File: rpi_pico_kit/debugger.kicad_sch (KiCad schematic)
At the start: 39 parts, among them J3 USB_B, U2 RP2040, U3 NCP1117-3.3_SOT223, U4 W25Q128JVS, Y1 12MHz

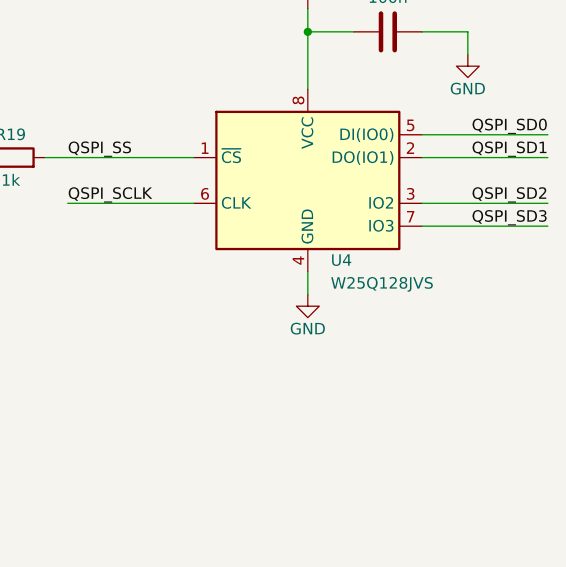
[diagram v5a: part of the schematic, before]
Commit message: added MPNs for capacitors
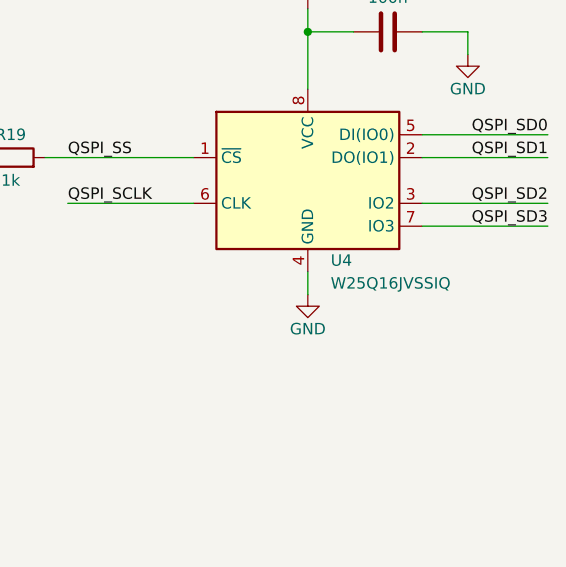
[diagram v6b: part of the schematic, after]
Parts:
- C10, C11, C12, C18, C3, C4, C6, C7, C8, C9: Manufacturer Part Number (none) -> C0805C104M3RAC7800; Supplier (none) -> Digikey; Supplier Part URL (none) -> https://www.digikey.cz/en/products/detail/kemet/C0805C104M3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
- C13, C5: Manufacturer Part Number (none) -> C0805C105Z4VAC7800; Supplier (none) -> Digikey; Supplier Part URL (none) -> https://www.digikey.cz/en/products/detail/kemet/C0805C105Z4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
- C14, C15: Manufacturer Part Number (none) -> C0805C120J1HAC7800; Supplier (none) -> Digikey; Supplier Part URL (none) -> https://www.digikey.cz/en/products/detail/kemet/C0805C120J1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
- C16, C17: Manufacturer Part Number (none) -> CL21A106KOQNNNG; Supplier (none) -> Digikey; Supplier Part URL (none) -> https://www.digikey.cz/en/products/detail/samsung-electro-m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
- U4: value W25Q128JVS -> W25Q16JVSSIQ; Manufacturer Part Number (none) -> W25Q16JVSSIQ; Supplier (none) -> Digikey; Supplier Part URL (none) -> https://www.digikey.cz/cs/products/detail/winbond-electroni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
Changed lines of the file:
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@@
+      (effects (font (size 1.27 1.27)) hide)
+    )
+    (property "Manufacturer Part Number" "C0805C104M3RAC7800" (id 4) (at 170.18 34.29 0)
+      (effects (font (size 1.27 1.27)) hide)
+    )
+    (property "Supplier" "Digikey" (id 5) (at 170.18 34.29 0)
+      (effects (font (size 1.27 1.27)) hide)
+    )
+    (property "Supplier Part URL" "https://www.digikey.cz/en/products/detail/kemet/C0805C104M3RAC7800/2211748" (id 6) (at 170.18 34.29 0)
       (effects (font (size 1.27 1.27)) hide)
     )
@@
       (effects (font (size 1.27 1.27)) hide)
     )
+    (property "Manufacturer Part Number" "C0805C104M3RAC7800" (id 4) (at 135.89 34.29 0)
+      (effects (font (size 1.27 1.27)) hide)
+    )
+    (property "Supplier" "Digikey" (id 5) (at 135.89 34.29 0)
+      (effects (font (size 1.27 1.27)) hide)
+    )
+    (property "Supplier Part URL" "https://www.digikey.cz/en/products/detail/kemet/C0805C104M3RAC7800/2211748" (id 6) (at 135.89 34.29 0)
+      (effects (font (size 1.27 1.27)) hide)
+    )
     (pin "1")
     (pin "2")
@@
       (effects (font (size 1.27 1.27)) hide)
     )
+    (property "Manufacturer Part Number" "C0805C104M3RAC7800" (id 4) (at 124.46 34.29 0)
+      (effects (font (size 1.27 1.27)) hide)
+    )
+    (property "Supplier" "Digikey" (id 5) (at 124.46 34.29 0)
+      (effects (font (size 1.27 1.27)) hide)
+    )
+    (property "Supplier Part URL" "https://www.digikey.cz/en/products/detail/kemet/C0805C104M3RAC7800/2211748" (id 6) (at 124.46 34.29 0)
+      (effects (font (size 1.27 1.27)) hide)
+    )
     (pin "1")
     (pin "2")
@@
       (effects (font (size 1.27 1.27)) hide)
     )
+    (property "Manufacturer Part Number" "C0805C104M3RAC7800" (id 4) (at 113.03 34.29 0)
+      (effects (font (size 1.27 1.27)) hide)
+    )
+    (property "Supplier" "Digikey" (id 5) (at 113.03 34.29 0)
+      (effects (font (size 1.27 1.27)) hide)
+    )
+    (property "Supplier Part URL" "https://www.digikey.cz/en/products/detail/kemet/C0805C104M3RAC7800/2211748" (id 6) (at 113.03 34.29 0)
+      (effects (font (size 1.27 1.27)) hide)
+    )
     (pin "1")
     (pin "2")
@@
     )
     (property "Datasheet" "~" (id 3) (at 44.45 48.26 0)
+      (effects (font (size 1.27 1.27)) hide)
+    )
+    (property "Manufacturer Part Number" "C0805C105Z4VAC7800" (id 4) (at 44.45 48.26 0)
+      (effects (font (size 1.27 1.27)) hide)
+    )
+    (property "Supplier" "Digikey" (id 5) (at 44.45 48.26 0)
+      (effects (font (size 1.27 1.27)) hide)
+    )
+    (property "Supplier Part URL" "https://www.digikey.cz/en/products/detail/kemet/C0805C105Z4VAC7800/2211782" (id 6) (at 44.45 48.26 0)
       (effects (font (size 1.27 1.27)) hide)
     )
@@
     )
     (property "Datasheet" "~" (id 3) (at 228.6 46.99 0)
+      (effects (font (size 1.27 1.27)) hide)
+    )
+    (property "Manufacturer Part Number" "CL21A106KOQNNNG" (id 4) (at 228.6 46.99 0)
+      (effects (font (size 1.27 1.27)) hide)
+    )
+    (property "Supplier" "Digikey" (id 5) (at 228.6 46.99 0)
+      (effects (font (size 1.27 1.27)) hide)
+    )
+    (property "Supplier Part URL" "https://www.digikey.cz/en/products/detail/samsung-electro-mechanics/CL21A106KOQNNNG/3894417" (id 6) (at 228.6 46.99 0)
       (effects (font (size 1.27 1.27)) hide)
     )
@@
       (effects (font (size 1.27 1.27)) hide)
     )
+    (property "Manufacturer Part Number" "C0805C104M3RAC7800" (id 4) (at 147.32 34.29 0)
+      (effects (font (size 1.27 1.27)) hide)
+    )
+    (property "Supplier" "Digikey" (id 5) (at 147.32 34.29 0)
+      (effects (font (size 1.27 1.27)) hide)
+    )
+    (property "Supplier Part URL" "https://www.digikey.cz/en/products/detail/kemet/C0805C104M3RAC7800/2211748" (id 6) (at 147.32 34.29 0)
+      (effects (font (size 1.27 1.27)) hide)
+    )
     (pin "1")
     (pin "2")
@@
       (effects (font (size 1.27 1.27)) hide)
     )
+    (property "Manufacturer Part Number" "C0805C104M3RAC7800" (id 4) (at 158.75 34.29 0)
+      (effects (font (size 1.27 1.27)) hide)
+    )
+    (property "Supplier" "Digikey" (id 5) (at 158.75 34.29 0)
+      (effects (font (size 1.27 1.27)) hide)
+    )
+    (property "Supplier Part URL" "https://www.digikey.cz/en/products/detail/kemet/C0805C104M3RAC7800/2211748" (id 6) (at 158.75 34.29 0)
+      (effects (font (size 1.27 1.27)) hide)
+    )
     (pin "1")
     (pin "2")
@@
       (effects (font (size 1.27 1.27)) hide)
     )
+    (property "Manufacturer Part Number" "C0805C120J1HAC7800" (id 4) (at 132.08 171.45 0)
+      (effects (font (size 1.27 1.27)) hide)
+    )
+    (property "Supplier" "Digikey" (id 5) (at 132.08 171.45 0)
+      (effects (font (size 1.27 1.27)) hide)
+    )
+    (property "Supplier Part URL" "https://www.digikey.cz/en/products/detail/kemet/C0805C120J1HAC7800/7948525" (id 6) (at 132.08 171.45 0)
+      (effects (font (size 1.27 1.27)) hide)
+    )
     (pin "1")
     (pin "2")
@@
     )
     (property "Datasheet" "~" (id 3) (at 101.6 34.29 0)
+      (effects (font (size 1.27 1.27)) hide)
+    )
+    (property "Manufacturer Part Number" "C0805C104M3RAC7800" (id 4) (at 101.6 34.29 0)
+      (effects (font (size 1.27 1.27)) hide)
+    )
+    (property "Supplier" "Digikey" (id 5) (at 101.6 34.29 0)
+      (effects (font (size 1.27 1.27)) hide)
+    )
+    (property "Supplier Part URL" "https://www.digikey.cz/en/products/detail/kemet/C0805C104M3RAC7800/2211748" (id 6) (at 101.6 34.29 0)
       (effects (font (size 1.27 1.27)) hide)
     )
@@
       (effects (font (size 1.27 1.27)) hide)
     )
+    (property "Manufacturer Part Number" "C0805C120J1HAC7800" (id 4) (at 132.08 184.15 0)
+      (effects (font (size 1.27 1.27)) hide)
+    )
+    (property "Supplier" "Digikey" (id 5) (at 132.08 184.15 0)
+      (effects (font (size 1.27 1.27)) hide)
+    )
+    (property "Supplier Part URL" "https://www.digikey.cz/en/products/detail/kemet/C0805C120J1HAC7800/7948525" (id 6) (at 132.08 184.15 0)
+      (effects (font (size 1.27 1.27)) hide)
+    )
     (pin "1")
     (pin "2")
@@
     )
     (property "Datasheet" "~" (id 3) (at 33.02 34.29 0)
+      (effects (font (size 1.27 1.27)) hide)
+    )
+    (property "Manufacturer Part Number" "C0805C104M3RAC7800" (id 4) (at 33.02 34.29 0)
+      (effects (font (size 1.27 1.27)) hide)
+    )
+    (property "Supplier" "Digikey" (id 5) (at 33.02 34.29 0)
+      (effects (font (size 1.27 1.27)) hide)
+    )
+    (property "Supplier Part URL" "https://www.digikey.cz/en/products/detail/kemet/C0805C104M3RAC7800/2211748" (id 6) (at 33.02 34.29 0)
       (effects (font (size 1.27 1.27)) hide)
     )
@@
       (effects (font (size 1.27 1.27)) hide)
     )
+    (property "Manufacturer Part Number" "C0805C104M3RAC7800" (id 4) (at 44.45 34.29 0)
+      (effects (font (size 1.27 1.27)) hide)
+    )
+    (property "Supplier" "Digikey" (id 5) (at 44.45 34.29 0)
+      (effects (font (size 1.27 1.27)) hide)
+    )
+    (property "Supplier Part URL" "https://www.digikey.cz/en/products/detail/kemet/C0805C104M3RAC7800/2211748" (id 6) (at 44.45 34.29 0)
+      (effects (font (size 1.27 1.27)) hide)
+    )
     (pin "1")
     (pin "2")
@@
       (effects (font (size 1.27 1.27)) hide)
     )
+    (property "Manufacturer Part Number" "CL21A106KOQNNNG" (id 4) (at 256.54 46.99 0)
+      (effects (font (size 1.27 1.27)) hide)
+    )
+    (property "Supplier" "Digikey" (id 5) (at 256.54 46.99 0)
+      (effects (font (size 1.27 1.27)) hide)
+    )
+    (property "Supplier Part URL" "https://www.digikey.cz/en/products/detail/samsung-electro-mechanics/CL21A106KOQNNNG/3894417" (id 6) (at 256.54 46.99 0)
+      (effects (font (size 1.27 1.27)) hide)
+    )
     (pin "1")
     (pin "2")
@@
       (effects (font (size 1.27 1.27)) hide)
     )
+    (property "Manufacturer Part Number" "C0805C104M3RAC7800" (id 4) (at 246.38 111.76 0)
+      (effects (font (size 1.27 1.27)) hide)
+    )
+    (property "Supplier" "Digikey" (id 5) (at 246.38 111.76 0)
+      (effects (font (size 1.27 1.27)) hide)
+    )
+    (property "Supplier Part URL" "https://www.digikey.cz/en/products/detail/kemet/C0805C104M3RAC7800/2211748" (id 6) (at 246.38 111.76 0)
+      (effects (font (size 1.27 1.27)) hide)
+    )
     (pin "1")
     (pin "2")
@@
     )
     (property "Datasheet" "~" (id 3) (at 101.6 48.26 0)
+      (effects (font (size 1.27 1.27)) hide)
+    )
+    (property "Manufacturer Part Number" "C0805C105Z4VAC7800" (id 4) (at 101.6 48.26 0)
+      (effects (font (size 1.27 1.27)) hide)
+    )
+    (property "Supplier" "Digikey" (id 5) (at 101.6 48.26 0)
+      (effects (font (size 1.27 1.27)) hide)
+    )
+    (property "Supplier Part URL" "https://www.digikey.cz/en/products/detail/kemet/C0805C105Z4VAC7800/2211782" (id 6) (at 101.6 48.26 0)
       (effects (font (size 1.27 1.27)) hide)
     )
@@
       (effects (font (size 1.27 1.27)) (justify left))
     )
-    (property "Value" "W25Q128JVS" (id 1) (at 240.03 139.7 0)
+    (property "Value" "W25Q16JVSSIQ" (id 1) (at 240.03 139.7 0)
       (effects (font (size 1.27 1.27)) (justify left))
     )
@@
       (effects (font (size 1.27 1.27)) hide)
     )
+    (property "Manufacturer Part Number" "W25Q16JVSSIQ" (id 4) (at 237.49 128.27 0)
+      (effects (font (size 1.27 1.27)) hide)
+    )
+    (property "Supplier" "Digikey" (id 5) (at 237.49 128.27 0)
+      (effects (font (size 1.27 1.27)) hide)
+    )
+    (property "Supplier Part URL" "https://www.digikey.cz/cs/products/detail/winbond-electronics/W25Q16JVSSIQ/6193769" (id 6) (at 237.49 128.27 0)
+      (effects (font (size 1.27 1.27)) hide)
+    )

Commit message: added MPNs for resistors
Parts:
- R10, R11: Manufacturer Part Number (none) -> RC0805FR-0727RL; Supplier (none) -> Digikey; Supplier Part URL (none) -> https://www.digikey.cz/en/products/detail/yageo/RC0805FR-07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
- R12, R13, R16, R17, R18, R19, R24, R27: Manufacturer Part Number (none) -> RC0805FR-071KL; Supplier (none) -> Digikey; Supplier Part URL (none) -> https://www.digikey.cz/en/products/detail/yageo/RC0805FR-07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
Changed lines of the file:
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@@
+      (effects (font (size 1.27 1.27)) hide)
+    )
+    (property "Manufacturer Part Number" "RC0805FR-071KL" (id 4) (at 154.94 184.15 0)
+      (effects (font (size 1.27 1.27)) hide)
+    )
+    (property "Supplier Part URL" "https://www.digikey.cz/en/products/detail/yageo/RC0805FR-071KL/727444" (id 5) (at 154.94 184.15 0)
+      (effects (font (size 1.27 1.27)) hide)
+    )
+    (property "Supplier" "Digikey" (id 6) (at 154.94 184.15 0)
       (effects (font (size 1.27 1.27)) hide)
     )
@@
     )
     (property "Datasheet" "~" (id 3) (at 120.65 67.31 0)
+      (effects (font (size 1.27 1.27)) hide)
+    )
+    (property "Manufacturer Part Number" "RC0805FR-0727RL" (id 4) (at 120.65 67.31 0)
+      (effects (font (size 1.27 1.27)) hide)
+    )
+    (property "Supplier Part URL" "https://www.digikey.cz/en/products/detail/yageo/RC0805FR-0727RL/727779" (id 5) (at 120.65 67.31 0)
+      (effects (font (size 1.27 1.27)) hide)
+    )
+    (property "Supplier" "Digikey" (id 6) (at 120.65 67.31 0)
       (effects (font (size 1.27 1.27)) hide)
     )
@@
       (effects (font (size 1.27 1.27)) hide)
     )
+    (property "Manufacturer Part Number" "RC0805FR-071KL" (id 4) (at 204.47 125.73 0)
+      (effects (font (size 1.27 1.27)) hide)
+    )
+    (property "Supplier Part URL" "https://www.digikey.cz/en/products/detail/yageo/RC0805FR-071KL/727444" (id 5) (at 204.47 125.73 0)
+      (effects (font (size 1.27 1.27)) hide)
+    )
+    (property "Supplier" "Digikey" (id 6) (at 204.47 125.73 0)
+      (effects (font (size 1.27 1.27)) hide)
+    )
     (pin "1")
     (pin "2")
@@
       (effects (font (size 1.27 1.27)) hide)
     )
+    (property "Manufacturer Part Number" "RC0805FR-071KL" (id 4) (at 125.73 140.97 0)
+      (effects (font (size 1.27 1.27)) hide)
+    )
+    (property "Supplier Part URL" "https://www.digikey.cz/en/products/detail/yageo/RC0805FR-071KL/727444" (id 5) (at 125.73 140.97 0)
+      (effects (font (size 1.27 1.27)) hide)
+    )
+    (property "Supplier" "Digikey" (id 6) (at 125.73 140.97 0)
+      (effects (font (size 1.27 1.27)) hide)
+    )
     (pin "1")
     (pin "2")
@@
     )
     (property "Datasheet" "~" (id 3) (at 120.65 80.01 0)
+      (effects (font (size 1.27 1.27)) hide)
+    )
+    (property "Manufacturer Part Number" "RC0805FR-071KL" (id 4) (at 120.65 80.01 0)
+      (effects (font (size 1.27 1.27)) hide)
+    )
+    (property "Supplier Part URL" "https://www.digikey.cz/en/products/detail/yageo/RC0805FR-071KL/727444" (id 5) (at 120.65 80.01 0)
+      (effects (font (size 1.27 1.27)) hide)
+    )
+    (property "Supplier" "Digikey" (id 6) (at 120.65 80.01 0)
       (effects (font (size 1.27 1.27)) hide)
     )
@@
       (effects (font (size 1.27 1.27)) hide)
     )
+    (property "Manufacturer Part Number" "RC0805FR-071KL" (id 4) (at 120.65 77.47 0)
+      (effects (font (size 1.27 1.27)) hide)
+    )
+    (property "Supplier Part URL" "https://www.digikey.cz/en/products/detail/yageo/RC0805FR-071KL/727444" (id 5) (at 120.65 77.47 0)
+      (effects (font (size 1.27 1.27)) hide)
+    )
+    (property "Supplier" "Digikey" (id 6) (at 120.65 77.47 0)
+      (effects (font (size 1.27 1.27)) hide)
+    )
     (pin "1")
     (pin "2")
@@
       (effects (font (size 1.27 1.27)) hide)
     )
+    (property "Manufacturer Part Number" "RC0805FR-0727RL" (id 4) (at 120.65 69.85 0)
+      (effects (font (size 1.27 1.27)) hide)
+    )
+    (property "Supplier Part URL" "https://www.digikey.cz/en/products/detail/yageo/RC0805FR-0727RL/727779" (id 5) (at 120.65 69.85 0)
+      (effects (font (size 1.27 1.27)) hide)
+    )
+    (property "Supplier" "Digikey" (id 6) (at 120.65 69.85 0)
+      (effects (font (size 1.27 1.27)) hide)
+    )
     (pin "1")
     (pin "2")
@@
       (effects (font (size 1.27 1.27)) hide)
     )
+    (property "Manufacturer Part Number" "RC0805FR-071KL" (id 4) (at 120.65 82.55 0)
+      (effects (font (size 1.27 1.27)) hide)
+    )
+    (property "Supplier Part URL" "https://www.digikey.cz/en/products/detail/yageo/RC0805FR-071KL/727444" (id 5) (at 120.65 82.55 0)
+      (effects (font (size 1.27 1.27)) hide)
+    )
+    (property "Supplier" "Digikey" (id 6) (at 120.65 82.55 0)
+      (effects (font (size 1.27 1.27)) hide)
+    )
     (pin "1")
     (pin "2")
@@
       (effects (font (size 1.27 1.27)) hide)
     )
+    (property "Manufacturer Part Number" "RC0805FR-071KL" (id 4) (at 120.65 85.09 0)
+      (effects (font (size 1.27 1.27)) hide)
+    )
+    (property "Supplier Part URL" "https://www.digikey.cz/en/products/detail/yageo/RC0805FR-071KL/727444" (id 5) (at 120.65 85.09 0)
+      (effects (font (size 1.27 1.27)) hide)
+    )
+    (property "Supplier" "Digikey" (id 6) (at 120.65 85.09 0)
+      (effects (font (size 1.27 1.27)) hide)
+    )
     (pin "1")
     (pin "2")
@@
       (effects (font (size 1.27 1.27)) hide)
     )
+    (property "Manufacturer Part Number" "RC0805FR-071KL" (id 4) (at 120.65 92.71 0)
+      (effects (font (size 1.27 1.27)) hide)
+    )
+    (property "Supplier Part URL" "https://www.digikey.cz/en/products/detail/yageo/RC0805FR-071KL/727444" (id 5) (at 120.65 92.71 0)
+      (effects (font (size 1.27 1.27)) hide)
+    )
+    (property "Supplier" "Digikey" (id 6) (at 120.65 92.71 0)
+      (effects (font (size 1.27 1.27)) hide)
+    )
